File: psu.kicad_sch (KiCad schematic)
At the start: 36 parts, among them U1 TLS115, U2 TLS115, U3 LMR14020, U4 MCP2551-I-SN, U5 MCP2551-I-SN, U6 AMS1117-3.3

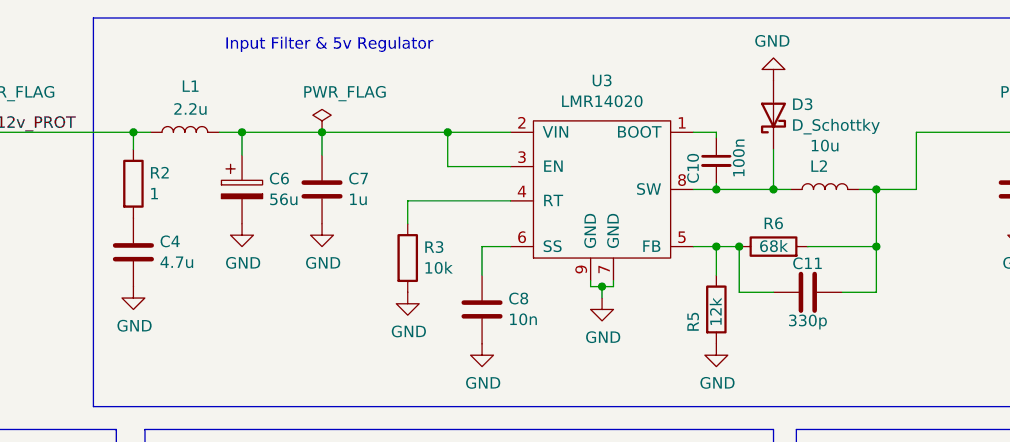
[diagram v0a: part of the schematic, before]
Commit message: Published 1.5 gerbs, bom, cpl and pdf
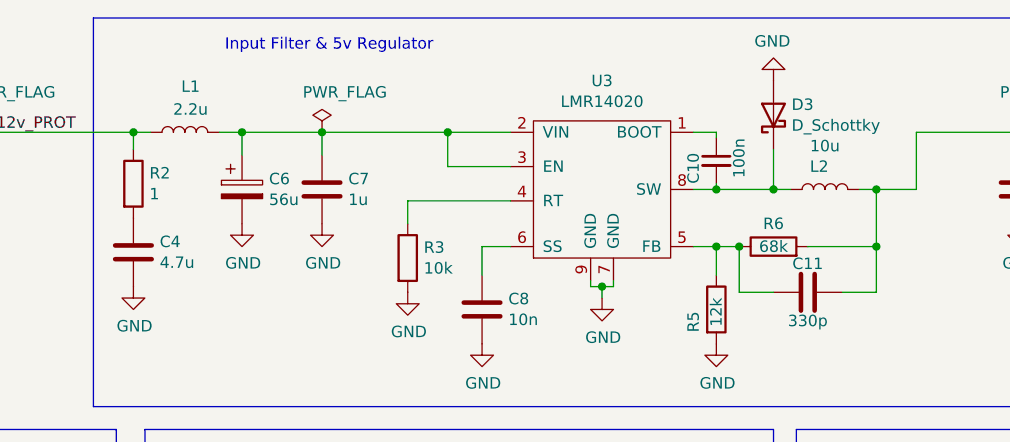
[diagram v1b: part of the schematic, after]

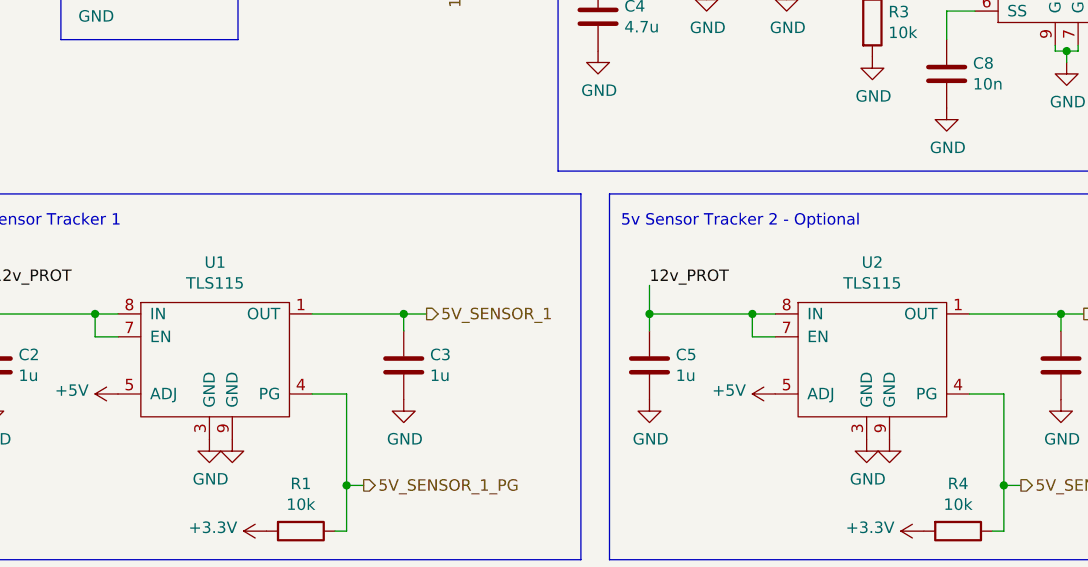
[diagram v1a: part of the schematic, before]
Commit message: make hardware updates: - fix erc/drc errors - switch to VNLD5090 - switch to SOIC8 ignition drivers - BOM deduplication of similar parts
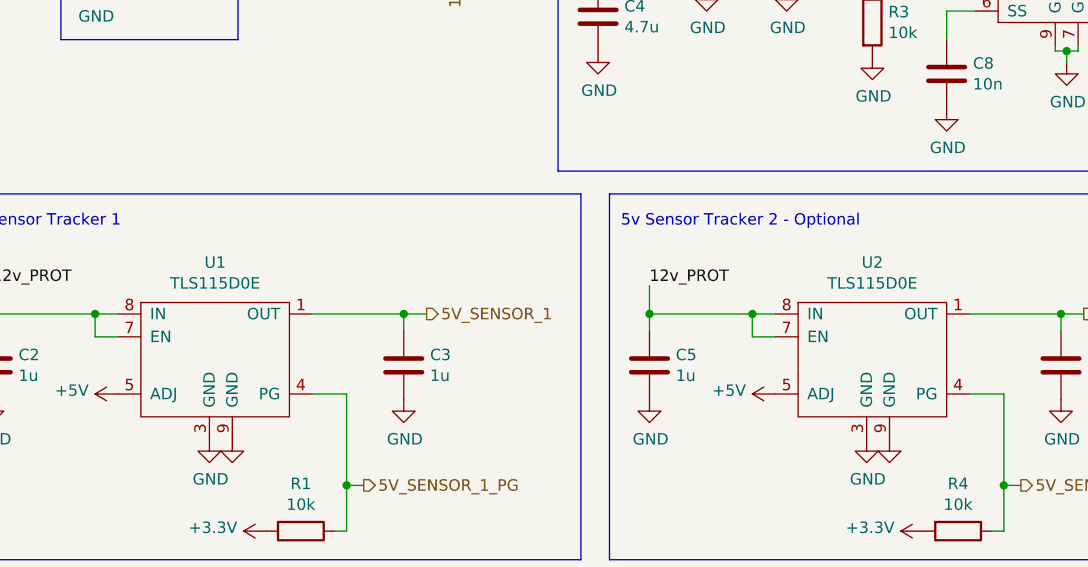
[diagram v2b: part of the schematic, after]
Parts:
- L1: LCSC C36828 -> C75646
- U1, U2: value TLS115 -> TLS115D0E; LCSC N/A -> C3747428
- U4, U5: LCSC (none) -> C7376
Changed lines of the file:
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@@
       (effects (font (size 1.27 1.27)) hide)
     )
-    (property "LCSC" "C36828" (at 93.345 29.21 0)
+    (property "LCSC" "C75646" (at 93.345 29.21 0)
       (effects (font (size 1.27 1.27)) hide)
     )
@@
       (effects (font (size 1.27 1.27)))
     )
-    (property "Value" "TLS115" (at 45.085 72.1614 0)
+    (property "Value" "TLS115D0E" (at 45.085 72.1614 0)
       (effects (font (size 1.27 1.27)))
     )
@@
       (effects (font (size 1.27 1.27)) hide)
     )
-    (property "LCSC" "N/A" (at 44.45 78.105 0)
+    (property "LCSC" "C3747428" (at 44.45 78.105 0)
       (effects (font (size 1.27 1.27)) hide)
     )
@@
       (effects (font (size 1.27 1.27)))
     )
-    (property "Value" "TLS115" (at 118.11 72.1614 0)
+    (property "Value" "TLS115D0E" (at 118.11 72.1614 0)
       (effects (font (size 1.27 1.27)))
     )
@@
       (effects (font (size 1.27 1.27)) hide)
     )
-    (property "LCSC" "N/A" (at 117.475 78.105 0)
+    (property "LCSC" "C3747428" (at 117.475 78.105 0)
       (effects (font (size 1.27 1.27)) hide)
     )
@@
       (effects (font (size 1.27 1.27)) hide)
     )
+    (property "LCSC" "C7376" (at 190.4992 125.056 0)
+      (effects (font (size 1.27 1.27)) hide)
+    )
     (pin "1")
     (pin "2")
@@
       (effects (font (size 1.27 1.27)) hide)
     )
+    (property "LCSC" "C7376" (at 190.4939 81.9312 0)
+      (effects (font (size 1.27 1.27)) hide)
+    )
